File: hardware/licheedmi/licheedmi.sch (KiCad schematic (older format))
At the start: 48 parts

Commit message: sch: Misc touches
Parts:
- removed D? (x3): RED, symbol Device:LED_Small
- added D? (x3): RED, LED_SMD:LED_0603_1608Metric, symbol Device:LED_Small
- D?: footprint (none) -> LED_SMD:LED_0603_1608Metric
- J?: footprint (none) -> hdmizness:HDMI_A_PCB
- J?: footprint (none) -> hdmizness:Boomelec_HDMI-001
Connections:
- net +3V3: now also D?.2 (A), D?.2 (A), D?.2 (A)
- net at R?.2: now also D?.1 (K) (x3)
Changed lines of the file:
@@
 encoding utf-8
 Sheet 1 1
-Title ""
-Date ""
-Rev ""
+Title "LicheeDMI"
+Date "2020-05-29"
+Rev "1"
 Comp ""
 Comment1 ""
 Comment2 ""
-Comment3 ""
-Comment4 ""
+Comment3 "through both a regular HDMI connector and a fully PCB-based one."
+Comment4 "Demo board to give HDMI output to Sipeed Lichee Nano SoM"
 $EndDescr
 $Comp
@@
 F 0 "J?" H 15330 3846 50  0000 L CNN
 F 1 "HDMI_A" H 15330 3755 50  0000 L CNN
-F 2 "" H 14925 3800 50  0001 C CNN
+F 2 "hdmizness:HDMI_A_PCB" H 14925 3800 50  0001 C CNN
 F 3 "https://en.wikipedia.org/wiki/HDMI" H 14925 3800 50  0001 C CNN
 	1    14900 3800
@@
 F 0 "J?" H 15330 6746 50  0000 L CNN
 F 1 "HDMI_A" H 15330 6655 50  0000 L CNN
-F 2 "" H 14925 6700 50  0001 C CNN
+F 2 "hdmizness:Boomelec_HDMI-001" H 14925 6700 50  0001 C CNN
 F 3 "https://en.wikipedia.org/wiki/HDMI" H 14925 6700 50  0001 C CNN
 	1    14900 6700
@@
 	-1   0    0    1
 $EndComp
-$Comp
-L Device:LED_Small D?
-U 1 1 5F6D70B3
-P 4700 3200
-F 0 "D?" V 5000 3250 50  0000 R CNN
-F 1 "RED" V 4900 3250 50  0000 R CNN
-F 2 "" V 4700 3200 50  0001 C CNN
-F 3 "~" V 4700 3200 50  0001 C CNN
-	1    4700 3200
-	0    -1   -1   0
-$EndComp
 Wire Wire Line
 	4700 3300 4700 3400
@@
 $Comp
 L Device:LED_Small D?
-U 1 1 5F6D6BCD
-P 4500 3200
-F 0 "D?" V 4800 3250 50  0000 R CNN
-F 1 "RED" V 4700 3250 50  0000 R CNN
-F 2 "" V 4500 3200 50  0001 C CNN
-F 3 "~" V 4500 3200 50  0001 C CNN
-	1    4500 3200
-	0    -1   -1   0
-$EndComp
-$Comp
-L Device:LED_Small D?
-U 1 1 5F6D655D
-P 4300 3200
-F 0 "D?" V 4600 3250 50  0000 R CNN
-F 1 "RED" V 4500 3250 50  0000 R CNN
-F 2 "" V 4300 3200 50  0001 C CNN
-F 3 "~" V 4300 3200 50  0001 C CNN
-	1    4300 3200
-	0    -1   -1   0
-$EndComp
-$Comp
-L Device:LED_Small D?
 U 1 1 5F6D3496
 P 4100 3200
 F 0 "D?" V 4400 3250 50  0000 R CNN
 F 1 "RED" V 4300 3250 50  0000 R CNN
-F 2 "" V 4100 3200 50  0001 C CNN
+F 2 "LED_SMD:LED_0603_1608Metric" V 4100 3200 50  0001 C CNN
 F 3 "~" V 4100 3200 50  0001 C CNN
 	1    4100 3200
@@
 Text Notes 11200 8600 0    50   ~ 0
 <-- Let me explain this monstruosity.\nHPD of the TDA19988 has a V_IH of 2V. Even\nwith the barely-in-spec HPD voltage of 4.8v,\nany of HPD_A or B getting there would raise\nHPD to 2.4v, making it a logic one in the chip's\neyes, effectively making an OR out of resistors.\n(Yeah too lazy to look for the proper 74 part)
+$Comp
+L Device:LED_Small D?
+U 1 1 613C01A5
+P 4300 3200
+F 0 "D?" V 4600 3250 50  0000 R CNN
+F 1 "RED" V 4500 3250 50  0000 R CNN
+F 2 "LED_SMD:LED_0603_1608Metric" V 4300 3200 50  0001 C CNN
+F 3 "~" V 4300 3200 50  0001 C CNN
+	1    4300 3200
+	0    -1   -1   0
+$EndComp
+$Comp
+L Device:LED_Small D?
+U 1 1 613C082E
+P 4500 3200
+F 0 "D?" V 4800 3250 50  0000 R CNN
+F 1 "RED" V 4700 3250 50  0000 R CNN
+F 2 "LED_SMD:LED_0603_1608Metric" V 4500 3200 50  0001 C CNN
+F 3 "~" V 4500 3200 50  0001 C CNN
+	1    4500 3200
+	0    -1   -1   0
+$EndComp
+$Comp
+L Device:LED_Small D?
+U 1 1 613C0C7E
+P 4700 3200
+F 0 "D?" V 5000 3250 50  0000 R CNN
+F 1 "RED" V 4900 3250 50  0000 R CNN
+F 2 "LED_SMD:LED_0603_1608Metric" V 4700 3200 50  0001 C CNN
+F 3 "~" V 4700 3200 50  0001 C CNN
+	1    4700 3200
+	0    -1   -1   0
+$EndComp
 $EndSCHEMATC

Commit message: sch: Add lots of testpoints
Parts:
- added J?: Conn_01x07, symbol Connector_Generic:Conn_01x07
- added R?: 0, Resistor_SMD:R_0603_1608Metric, symbol Device:R_Small
- added R?: DNP, Resistor_SMD:R_0603_1608Metric, symbol Device:R_Small
- added TP?: VDDC, symbol Connector:TestPoint
- added TP?: VDDATX, symbol Connector:TestPoint
- added TP?: VDDAPLL, symbol Connector:TestPoint
- added TP?: +1V8, symbol Connector:TestPoint
- added TP?: SCL_PCB, symbol Connector:TestPoint
- added TP?: SDA_PCB, symbol Connector:TestPoint
- added TP?: HPD_PCB, symbol Connector:TestPoint
- added TP?: SDA_FEM, symbol Connector:TestPoint
- added TP?: SCL_FEM, symbol Connector:TestPoint
- added TP?: HPD_FEM, symbol Connector:TestPoint
- added TP?: CEC_PCB, symbol Connector:TestPoint
- added TP?: CEC_FEM, symbol Connector:TestPoint
- added TP?: HPD, symbol Connector:TestPoint
- added TP?: SDA, symbol Connector:TestPoint
- added TP?: SCL, symbol Connector:TestPoint
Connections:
- net +1V8: now also TP?.1
- net CPU_SCL: now also TP?.1
- net CPU_SDA: now also TP?.1
- net GND: now also J?.1 (Pin_1)
- net HDCEC_FEM: now also TP?.1
- net HDCEC_PCB: now also TP?.1
- net HDSCL_FEM: now also TP?.1
- net HDSCL_PCB: now also TP?.1
- net HDSDA_FEM: now also TP?.1
- net HDSDA_PCB: now also TP?.1
- net HPD: now also TP?.1
- net HPD_A: now also TP?.1; no longer J?.19 (HPD), R?.1, R?.2, U?.27 (SEL)
- net HPD_B: now also TP?.1; no longer J?.19 (HPD), R?.1
- net RX0: now also J?.3 (Pin_3)
- net RX1: now also J?.5 (Pin_5)
- net RX2: now also J?.7 (Pin_7)
- net TX0: now also J?.2 (Pin_2)
- net TX1: now also J?.4 (Pin_4)
- net TX2: now also J?.6 (Pin_6)
- net VDDA: now also TP?.1
- net VDDAPLL: now also TP?.1
- net VDDATX: now also TP?.1
- new net HPD_FEM: J?.19 (HPD), R?.1, R?.1
- new net HPD_PCB: J?.19 (HPD), R?.1, R?.1
- new net OUT_SEL: R?.2, R?.2, R?.2, U?.27 (SEL)
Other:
- moved on the sheet: R?

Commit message: sch: Part number assignment done
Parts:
- C1, C11, C12, C13, C15, C16, C3, C4, C5, C6, C7: renamed from C?; LCSC P/N (none) -> C1591; MFR P/N (none) -> CL10B104KB8NNNC
- C10, C14, C2, C8, C9: renamed from C?; LCSC P/N (none) -> C95843; MFR P/N (none) -> CL10B105KP8NNNC
- D1, D2, D3, D4: renamed from D?; LCSC P/N (none) -> C157741; MFR P/N (none) -> LTST-C193KRKT-5A
- FB1, FB2, FB3: renamed from FB?; LCSC P/N (none) -> C136491; MFR P/N (none) -> MMZ1608Y601BTA00
- J1: renamed from J?; footprint (none) -> Connector_PinHeader_2.54mm:PinHeader_1x07_P2.54mm_Vertical; LCSC P/N (none) -> C225482; MFR P/N (none) -> A2541WV-7P
- J3: renamed from J?; LCSC P/N (none) -> C202114; MFR P/N (none) -> FH12-40S-0.5SH(55)
- J4: renamed from J?; LCSC P/N (none) -> C138388; MFR P/N (none) -> HDMI-001
- R1, R10, R11, R12, R14, R15, R19, R2, R20, R5, R6, R7, R8, R9: renamed from R?; LCSC P/N (none) -> C380759; MFR P/N (none) -> SY0603JN1KP
- R13, R16, R3, R4: renamed from R?; LCSC P/N (none) -> C98220; MFR P/N (none) -> RC0603FR-0710KL
- R18: renamed from R?; LCSC P/N (none) -> C132607; MFR P/N (none) -> WR06X000PTL
- TP1, TP10, TP11, TP12, TP13, TP14, TP15, TP2, TP3, TP4, TP5, TP6, TP7, TP8, TP9: renamed from TP?; footprint (none) -> TestPoint:TestPoint_Pad_D1.0mm
- U1: renamed from U?; MFR P/N (none) -> TDA19988BHN/C1,557; Newark P/N (none) -> 31AC7073
- U3: renamed from U?; LCSC P/N (none) -> C130083; MFR P/N (none) -> TS3DV20812RHHR
- gave numbers to parts that had none: 4

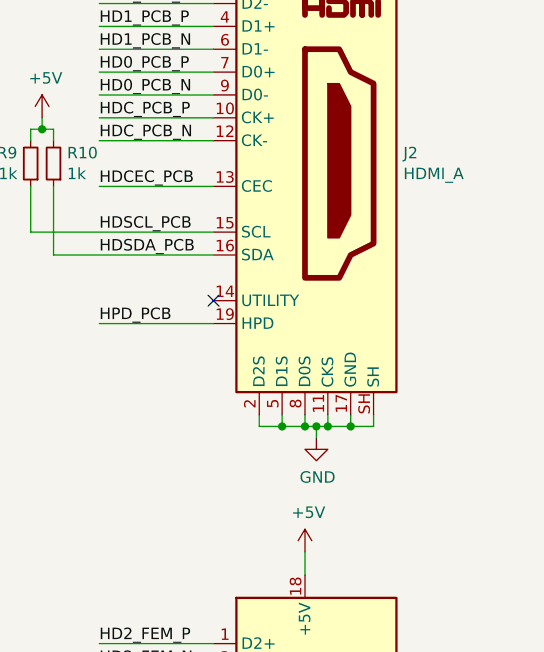
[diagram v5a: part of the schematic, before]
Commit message: sch: Add symbol for the PCB-based HDMI connector
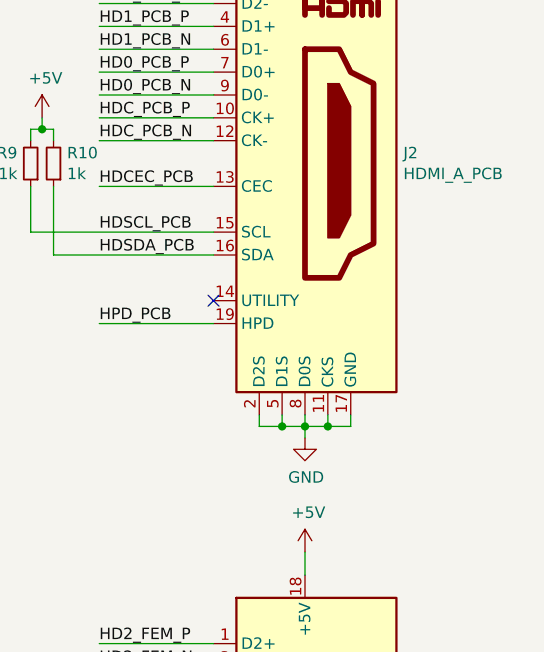
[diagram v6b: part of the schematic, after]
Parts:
- removed J2: HDMI_A, hdmizness:HDMI_A_PCB, symbol Connector:HDMI_A
- added J2: HDMI_A_PCB, hdmizness:HDMI_A_PCB, symbol hdmizness:HDMI_A_PCB
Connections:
- net +5V: now also J2.18 (+5V)
- net GND: now also J2.11 (CKS), J2.17 (GND), J2.2 (D2S), J2.5 (D1S), J2.8 (D0S)
- net HD0_PCB_N: now also J2.9 (D0-)
- net HD0_PCB_P: now also J2.7 (D0+)
- net HD1_PCB_N: now also J2.6 (D1-)
- net HD1_PCB_P: now also J2.4 (D1+)
- net HD2_PCB_N: now also J2.3 (D2-)
- net HD2_PCB_P: now also J2.1 (D2+)
- net HDCEC_PCB: now also J2.13 (CEC)
- net HDC_PCB_N: now also J2.12 (CK-)
- net HDC_PCB_P: now also J2.10 (CK+)
- net HDSCL_PCB: now also J2.15 (SCL)
- net HDSDA_PCB: now also J2.16 (SDA)
- net HPD_PCB: now also J2.19 (HPD)
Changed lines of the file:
@@
-$EndComp
-$Comp
-L Connector:HDMI_A J2
-U 1 1 5ED03A06
-P 14900 3800
-F 0 "J2" H 15330 3846 50  0000 L CNN
-F 1 "HDMI_A" H 15330 3755 50  0000 L CNN
-F 2 "hdmizness:HDMI_A_PCB" H 14925 3800 50  0001 C CNN
-F 3 "https://en.wikipedia.org/wiki/HDMI" H 14925 3800 50  0001 C CNN
-	1    14900 3800
-	1    0    0    -1
 $EndComp
 $Comp
@@
 	14700 4950 14800 4950
 Wire Wire Line
-	15200 4950 15200 4900
-Wire Wire Line
 	14800 4900 14800 4950
 Connection ~ 14800 4950
@@
 Connection ~ 14900 4950
 Wire Wire Line
-	14900 4950 14950 4950
-Wire Wire Line
 	15000 4900 15000 4950
 Connection ~ 15000 4950
@@
 Wire Wire Line
 	15100 4900 15100 4950
-Connection ~ 15100 4950
-Wire Wire Line
-	15100 4950 15200 4950
-Wire Wire Line
-	14950 4950 14950 5000
-Connection ~ 14950 4950
-Wire Wire Line
-	14950 4950 15000 4950
+Wire Wire Line
+	14900 4950 14900 5000
 $Comp
 L power:GND #PWR014
 U 1 1 5EE3E7C3
-P 14950 5000
-F 0 "#PWR014" H 14950 4750 50  0001 C CNN
-F 1 "GND" H 14955 4827 50  0000 C CNN
-F 2 "" H 14950 5000 50  0001 C CNN
-F 3 "" H 14950 5000 50  0001 C CNN
-	1    14950 5000
+P 14900 5000
+F 0 "#PWR014" H 14900 4750 50  0001 C CNN
+F 1 "GND" H 14905 4827 50  0000 C CNN
+F 2 "" H 14900 5000 50  0001 C CNN
+F 3 "" H 14900 5000 50  0001 C CNN
+	1    14900 5000
 	1    0    0    -1
 $EndComp
@@
 Wire Wire Line
 	10300 8100 10300 8150
+$Comp
+L hdmizness:HDMI_A_PCB J2
+U 1 1 61ECDFC8
+P 14900 3800
+F 0 "J2" H 15330 3846 50  0000 L CNN
+F 1 "HDMI_A_PCB" H 15330 3755 50  0000 L CNN
+F 2 "hdmizness:HDMI_A_PCB" H 14925 3800 50  0001 C CNN
+F 3 "https://en.wikipedia.org/wiki/HDMI" H 14925 3800 50  0001 C CNN
+	1    14900 3800
+	1    0    0    -1
+$EndComp
+Wire Wire Line
+	14900 4950 15000 4950
 $EndSCHEMATC

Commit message: pcb: Placement done
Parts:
- removed C13, C16: 100n, Capacitor_SMD:C_0603_1608Metric, symbol Device:C_Small
- TP1: value CEC_PCB -> CEC
- TP2: value SCL_PCB -> SCL
- TP3: value SDA_PCB -> SDA
- TP4: value HPD_PCB -> HPD
- TP5: value CEC_FEM -> CEC
- TP6: value SCL_FEM -> SCL
- TP7: value SDA_FEM -> SDA
- TP8: value HPD_FEM -> HPD
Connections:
- net HPD_A is gone; now on net HPD_PCB: TP4.1
- net HPD_B is gone; now on net HPD_FEM: TP8.1
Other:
- note added: "Common"
- note added: "PCB-based"
- note added: "Real"
- note added: "Write on PCB which one\nis which..."
- moved on the sheet: TP14, TP15
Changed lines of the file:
@@
 Wire Wire Line
 	3800 8800 3800 8900
-Text Label 5250 8900 2    50   ~ 0
+Text Label 5050 8900 2    50   ~ 0
 VDDATX
 $Comp
 L power:GND #PWR034
 U 1 1 5FDE31F0
-P 4500 9300
-F 0 "#PWR034" H 4500 9050 50  0001 C CNN
-F 1 "GND" H 4505 9127 50  0000 C CNN
-F 2 "" H 4500 9300 50  0001 C CNN
-F 3 "" H 4500 9300 50  0001 C CNN
-	1    4500 9300
+P 4400 9300
+F 0 "#PWR034" H 4400 9050 50  0001 C CNN
+F 1 "GND" H 4405 9127 50  0000 C CNN
+F 2 "" H 4400 9300 50  0001 C CNN
+F 3 "" H 4400 9300 50  0001 C CNN
+	1    4400 9300
 	1    0    0    -1
 $EndComp
@@
 	1    0    0    -1
 $EndComp
-$Comp
-L Device:C_Small C13
-U 1 1 60043CAC
-P 4800 9100
-F 0 "C13" H 4850 9450 50  0000 R CNN
-F 1 "100n" H 4800 9350 50  0000 C CNN
-F 2 "Capacitor_SMD:C_0603_1608Metric" H 4800 9100 50  0001 C CNN
-F 3 "~" H 4800 9100 50  0001 C CNN
-F 4 "C1591" H 4800 9100 50  0001 C CNN "LCSC P/N"
-F 5 "CL10B104KB8NNNC" H 4800 9100 50  0001 C CNN "MFR P/N"
-	1    4800 9100
-	1    0    0    -1
-$EndComp
 Wire Wire Line
 	4200 8900 4400 8900
@@
 	4600 8900 4600 9000
 Connection ~ 4400 8900
-Wire Wire Line
-	4800 8900 4800 9000
 Connection ~ 4600 8900
 Wire Wire Line
-	4600 8900 4800 8900
-Wire Wire Line
 	4200 9200 4200 9250
 Wire Wire Line
 	4200 9250 4400 9250
 Wire Wire Line
-	4800 9250 4800 9200
-Wire Wire Line
 	4600 9200 4600 9250
-Connection ~ 4600 9250
-Wire Wire Line
-	4600 9250 4800 9250
 Wire Wire Line
 	4400 9250 4400 9200
 Connection ~ 4400 9250
 Wire Wire Line
-	4400 9250 4500 9250
-Wire Wire Line
-	4500 9300 4500 9250
-Connection ~ 4500 9250
-Wire Wire Line
-	4500 9250 4600 9250
-Wire Wire Line
-	4800 8900 5250 8900
-Connection ~ 4800 8900
+	4400 9300 4400 9250
 $Comp
 L Device:C_Small C14
@@
 	1    0    0    -1
 $EndComp
-Text Label 5050 9750 2    50   ~ 0
+Text Label 4900 9750 2    50   ~ 0
 VDDAPLL
 $Comp
 L power:GND #PWR036
 U 1 1 601EC6F9
-P 4400 10150
-F 0 "#PWR036" H 4400 9900 50  0001 C CNN
-F 1 "GND" H 4405 9977 50  0000 C CNN
-F 2 "" H 4400 10150 50  0001 C CNN
-F 3 "" H 4400 10150 50  0001 C CNN
-	1    4400 10150
+P 4300 10150
+F 0 "#PWR036" H 4300 9900 50  0001 C CNN
+F 1 "GND" H 4305 9977 50  0000 C CNN
+F 2 "" H 4300 10150 50  0001 C CNN
+F 3 "" H 4300 10150 50  0001 C CNN
+	1    4300 10150
 	1    0    0    -1
 $EndComp
@@
 Wire Wire Line
 	4200 9750 4200 9850
-$Comp
-L Device:C_Small C16
-U 1 1 601EC708
-P 4600 9950
-F 0 "C16" H 4650 10300 50  0000 R CNN
-F 1 "100n" H 4600 10200 50  0000 C CNN
-F 2 "Capacitor_SMD:C_0603_1608Metric" H 4600 9950 50  0001 C CNN
-F 3 "~" H 4600 9950 50  0001 C CNN
-F 4 "C1591" H 4600 9950 50  0001 C CNN "LCSC P/N"
-F 5 "CL10B104KB8NNNC" H 4600 9950 50  0001 C CNN "MFR P/N"
-	1    4600 9950
-	1    0    0    -1
-$EndComp
 Wire Wire Line
 	4400 9750 4400 9850
-Wire Wire Line
-	4400 9750 4600 9750
-Wire Wire Line
-	4600 9750 4600 9850
 Connection ~ 4400 9750
-Connection ~ 4600 9750
 Wire Wire Line
 	4200 10050 4200 10100
 Wire Wire Line
-	4200 10100 4400 10100
-Wire Wire Line
-	4600 10050 4600 10100
+	4200 10100 4300 10100
 Wire Wire Line
 	4400 10100 4400 10050
-Connection ~ 4400 10100
-Wire Wire Line
-	4400 10150 4400 10100
-Wire Wire Line
-	4600 9750 5050 9750
-Wire Wire Line
-	4400 10100 4600 10100
+Wire Wire Line
+	4300 10150 4300 10100
 $Comp
 L Device:C_Small C2
@@
 L Connector:TestPoint TP14
 U 1 1 615688A4
-P 5250 8900
-F 0 "TP14" V 5204 9088 50  0000 L CNN
-F 1 "VDDATX" V 5295 9088 50  0000 L CNN
-F 2 "TestPoint:TestPoint_Pad_D1.0mm" H 5450 8900 50  0001 C CNN
-F 3 "~" H 5450 8900 50  0001 C CNN
-	1    5250 8900
+P 5050 8900
+F 0 "TP14" V 5004 9088 50  0000 L CNN
+F 1 "VDDATX" V 5095 9088 50  0000 L CNN
+F 2 "TestPoint:TestPoint_Pad_D1.0mm" H 5250 8900 50  0001 C CNN
+F 3 "~" H 5250 8900 50  0001 C CNN
+	1    5050 8900
 	0    1    1    0
 $EndComp
@@
 L Connector:TestPoint TP15
 U 1 1 61568FAC
-P 5050 9750
-F 0 "TP15" V 5004 9938 50  0000 L CNN
-F 1 "VDDAPLL" V 5095 9938 50  0000 L CNN
-F 2 "TestPoint:TestPoint_Pad_D1.0mm" H 5250 9750 50  0001 C CNN
-F 3 "~" H 5250 9750 50  0001 C CNN
-	1    5050 9750
+P 4900 9750
+F 0 "TP15" V 4854 9938 50  0000 L CNN
+F 1 "VDDAPLL" V 4945 9938 50  0000 L CNN
+F 2 "TestPoint:TestPoint_Pad_D1.0mm" H 5100 9750 50  0001 C CNN
+F 3 "~" H 5100 9750 50  0001 C CNN
+	1    4900 9750
 	0    1    1    0
 $EndComp
@@
 P 14650 1050
 F 0 "TP3" V 14696 1237 50  0001 L CNN
-F 1 "SDA_PCB" V 14650 1250 50  0000 L CNN
+F 1 "SDA" V 14650 1250 50  0000 L CNN
 F 2 "TestPoint:TestPoint_Pad_D1.0mm" H 14850 1050 50  0001 C CNN
 F 3 "~" H 14850 1050 50  0001 C CNN
@@
 P 14650 950
 F 0 "TP2" V 14696 1137 50  0001 L CNN
-F 1 "SCL_PCB" V 14650 1150 50  0000 L CNN
+F 1 "SCL" V 14650 1150 50  0000 L CNN
 F 2 "TestPoint:TestPoint_Pad_D1.0mm" H 14850 950 50  0001 C CNN
 F 3 "~" H 14850 950 50  0001 C CNN
@@
 P 14650 1150
 F 0 "TP4" V 14696 1337 50  0001 L CNN
-F 1 "HPD_PCB" V 14650 1350 50  0000 L CNN
+F 1 "HPD" V 14650 1350 50  0000 L CNN
 F 2 "TestPoint:TestPoint_Pad_D1.0mm" H 14850 1150 50  0001 C CNN
 F 3 "~" H 14850 1150 50  0001 C CNN
@@
 P 14650 1350
 F 0 "TP6" V 14696 1537 50  0001 L CNN
-F 1 "SCL_FEM" V 14650 1550 50  0000 L CNN
+F 1 "SCL" V 14650 1550 50  0000 L CNN
 F 2 "TestPoint:TestPoint_Pad_D1.0mm" H 14850 1350 50  0001 C CNN
 F 3 "~" H 14850 1350 50  0001 C CNN
@@
 P 14650 1450
 F 0 "TP7" V 14696 1637 50  0001 L CNN
-F 1 "SDA_FEM" V 14650 1650 50  0000 L CNN
+F 1 "SDA" V 14650 1650 50  0000 L CNN
 F 2 "TestPoint:TestPoint_Pad_D1.0mm" H 14850 1450 50  0001 C CNN
 F 3 "~" H 14850 1450 50  0001 C CNN
@@
 P 14650 1550
 F 0 "TP8" V 14696 1737 50  0001 L CNN
-F 1 "HPD_FEM" V 14650 1750 50  0000 L CNN
+F 1 "HPD" V 14650 1750 50  0000 L CNN
 F 2 "TestPoint:TestPoint_Pad_D1.0mm" H 14850 1550 50  0001 C CNN
 F 3 "~" H 14850 1550 50  0001 C CNN
@@
 P 14650 850
 F 0 "TP1" V 14696 1037 50  0001 L CNN
-F 1 "CEC_PCB" V 14650 1050 50  0000 L CNN
+F 1 "CEC" V 14650 1050 50  0000 L CNN
 F 2 "TestPoint:TestPoint_Pad_D1.0mm" H 14850 850 50  0001 C CNN
 F 3 "~" H 14850 850 50  0001 C CNN
@@
 P 14650 1250
 F 0 "TP5" V 14696 1437 50  0001 L CNN
-F 1 "CEC_FEM" V 14650 1450 50  0000 L CNN
+F 1 "CEC" V 14650 1450 50  0000 L CNN
 F 2 "TestPoint:TestPoint_Pad_D1.0mm" H 14850 1250 50  0001 C CNN
 F 3 "~" H 14850 1250 50  0001 C CNN
@@
 	15150 1050 14650 1050
 Text Label 15150 1150 2    50   ~ 0
-HPD_A
+HPD_PCB
 Wire Wire Line
 	15150 1150 14650 1150
@@
 	15150 1450 14650 1450
 Text Label 15150 1550 2    50   ~ 0
-HPD_B
+HPD_FEM
 Wire Wire Line
 	15150 1550 14650 1550
-Wire Wire Line
-	14650 1650 15150 1650
-Text Label 15150 1650 2    50   ~ 0
-HPD
-$Comp
-L Connector:TestPoint TP9
-U 1 1 61AB4CB2
-P 14650 1650
-F 0 "TP9" V 14696 1837 50  0001 L CNN
-F 1 "HPD" V 14650 1850 50  0000 L CNN
-F 2 "TestPoint:TestPoint_Pad_D1.0mm" H 14850 1650 50  0001 C CNN
-F 3 "~" H 14850 1650 50  0001 C CNN
-	1    14650 1650
-	0    -1   -1   0
-$EndComp
-$Comp
-L Connector:TestPoint TP11
-U 1 1 61B1F80E
-P 14650 1850
-F 0 "TP11" V 14696 2037 50  0001 L CNN
-F 1 "SDA" V 14650 2050 50  0000 L CNN
-F 2 "TestPoint:TestPoint_Pad_D1.0mm" H 14850 1850 50  0001 C CNN
-F 3 "~" H 14850 1850 50  0001 C CNN
-	1    14650 1850
-	0    -1   -1   0
-$EndComp
-$Comp
-L Connector:TestPoint TP10
-U 1 1 61B1F814
-P 14650 1750
-F 0 "TP10" V 14696 1937 50  0001 L CNN
-F 1 "SCL" V 14650 1950 50  0000 L CNN
-F 2 "TestPoint:TestPoint_Pad_D1.0mm" H 14850 1750 50  0001 C CNN
-F 3 "~" H 14850 1750 50  0001 C CNN
-	1    14650 1750
-	0    -1   -1   0
-$EndComp
-Text Label 15150 1850 2    50   ~ 0
-CPU_SDA
-Text Label 15150 1750 2    50   ~ 0
-CPU_SCL
-Wire Wire Line
-	15150 1750 14650 1750
-Wire Wire Line
-	15150 1850 14650 1850
 Text Notes 11200 8950 0    50   ~ 0
 <-- Let me explain this monstruosity.\nHPD of the TDA19988 has a V_IH of 2V. Even\nwith the barely-in-spec HPD voltage of 4.8v,\nany of HPD_A or B getting there would raise\nHPD to 2.4v, making it a logic one in the chip's\neyes, effectively making an OR out of resistors.\n(Yeah too lazy to look for the proper 74 part)
@@
 Wire Wire Line
 	14900 4950 15000 4950
+Text Notes 13350 2150 0    50   ~ 0
+Write on PCB which one\nis which...
+Text Notes 14150 1050 2    50   ~ 0
+PCB-based
+Text Notes 14150 1350 2    50   ~ 0
+Real
+Wire Wire Line
+	15150 1850 14650 1850
+Wire Wire Line
+	15150 1750 14650 1750
+Text Label 15150 1750 2    50   ~ 0
+CPU_SCL
+Text Label 15150 1850 2    50   ~ 0
+CPU_SDA
+$Comp
+L Connector:TestPoint TP10
+U 1 1 61B1F814
+P 14650 1750
+F 0 "TP10" V 14696 1937 50  0001 L CNN
+F 1 "SCL" V 14650 1950 50  0000 L CNN
+F 2 "TestPoint:TestPoint_Pad_D1.0mm" H 14850 1750 50  0001 C CNN
+F 3 "~" H 14850 1750 50  0001 C CNN
+	1    14650 1750
+	0    -1   -1   0
+$EndComp
+$Comp
+L Connector:TestPoint TP11
+U 1 1 61B1F80E
+P 14650 1850
+F 0 "TP11" V 14696 2037 50  0001 L CNN
+F 1 "SDA" V 14650 2050 50  0000 L CNN
+F 2 "TestPoint:TestPoint_Pad_D1.0mm" H 14850 1850 50  0001 C CNN
+F 3 "~" H 14850 1850 50  0001 C CNN
+	1    14650 1850
+	0    -1   -1   0
+$EndComp
+$Comp
+L Connector:TestPoint TP9
+U 1 1 61AB4CB2
+P 14650 1650
+F 0 "TP9" V 14696 1837 50  0001 L CNN
+F 1 "HPD" V 14650 1850 50  0000 L CNN
+F 2 "TestPoint:TestPoint_Pad_D1.0mm" H 14850 1650 50  0001 C CNN
+F 3 "~" H 14850 1650 50  0001 C CNN
+	1    14650 1650
+	0    -1   -1   0
+$EndComp
+Text Label 15150 1650 2    50   ~ 0
+HPD
+Wire Wire Line
+	14650 1650 15150 1650
+Text Notes 14150 1800 2    50   ~ 0
+Common
+Wire Notes Line
+	14100 1050 14100 1150
+Wire Notes Line
+	14100 1150 14125 1175
+Wire Notes Line
+	14100 1225 14125 1200
+Wire Notes Line
+	14100 1625 14125 1600
+Wire Notes Line
+	14125 1575 14100 1550
+Wire Notes Line
+	14125 1875 14100 1850
+Wire Notes Line
+	14100 1850 14100 1800
+Wire Notes Line
+	14100 1625 14100 1725
+Wire Notes Line
+	14100 1550 14100 1350
+Wire Notes Line
+	14100 1225 14100 1275
+Wire Notes Line
+	14100 825  14125 800
+Wire Notes Line
+	14100 825  14100 1000
+Wire Wire Line
+	4600 8900 5050 8900
+Wire Wire Line
+	4400 9750 4900 9750
+Wire Wire Line
+	4400 9250 4600 9250
+Connection ~ 4300 10100
+Wire Wire Line
+	4300 10100 4400 10100
 $EndSCHEMATC
